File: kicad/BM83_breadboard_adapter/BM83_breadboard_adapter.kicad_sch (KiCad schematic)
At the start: 66 parts, among them J1 PJ-320B, J2 PJ-320B, J3 USB_B_Micro, J4 Conn_01x25_Female, J5 Conn_01x25_Female, J6 PJ-320B, SW1 VOL-, SW2 VOL+, SW3 REV, SW4 FWD, SW6 PLAY/PAUSE, SW7 SELECT, SW8 MFB, SW9 RESET, U1 BM83, U2 PJ-3027F

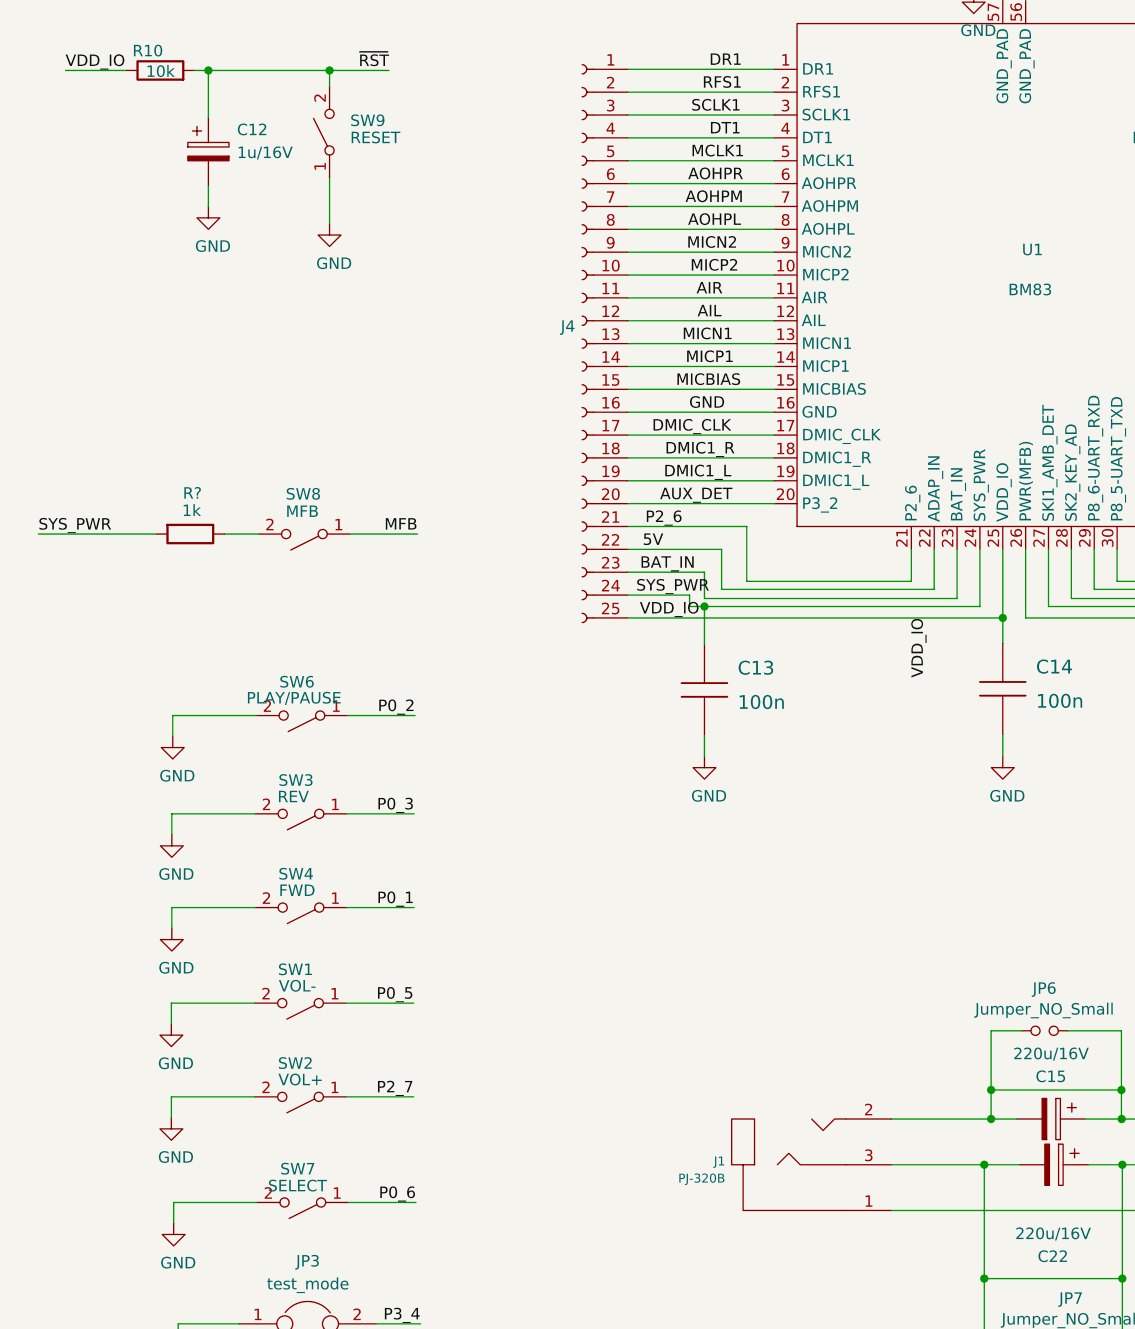
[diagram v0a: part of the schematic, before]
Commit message: update BM83 footprint on board!
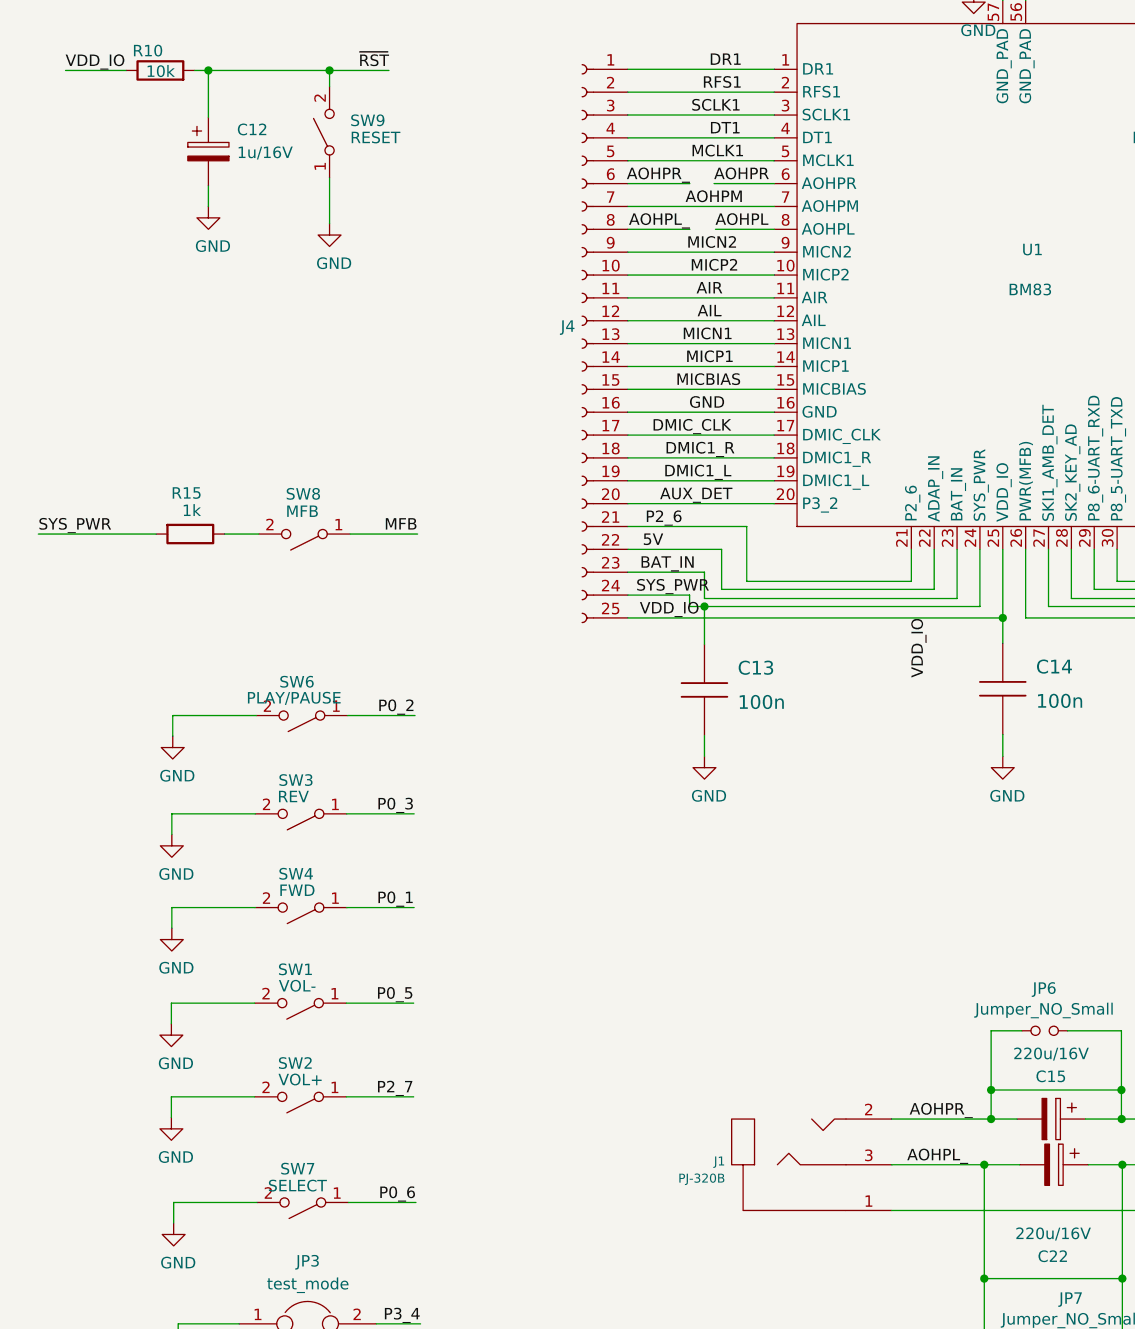
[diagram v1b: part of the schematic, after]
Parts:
- gave numbers to parts that had none: 1
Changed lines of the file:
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@@
     (stroke (width 0) (type solid) (color 0 0 0 0))
   )
-  (wire (pts (xy 294.7162 43.942) (xy 310.9722 43.942))
+  (wire (pts (xy 294.7162 43.942) (xy 301.5996 43.942))
     (stroke (width 0) (type solid) (color 0 0 0 0))
   )
@@
     (stroke (width 0) (type solid) (color 0 0 0 0))
   )
-  (wire (pts (xy 294.7162 49.022) (xy 310.9722 49.022))
+  (wire (pts (xy 294.7162 49.022) (xy 301.5996 49.022))
     (stroke (width 0) (type solid) (color 0 0 0 0))
   )
@@
   )
   (wire (pts (xy 303.2252 105.283) (xy 303.2252 107.569))
+    (stroke (width 0) (type solid) (color 0 0 0 0))
+  )
+  (wire (pts (xy 304.292 43.942) (xy 310.9722 43.942))
+    (stroke (width 0) (type solid) (color 0 0 0 0))
+  )
+  (wire (pts (xy 304.4444 49.022) (xy 310.9722 49.022))
     (stroke (width 0) (type solid) (color 0 0 0 0))
   )
@@
     (effects (font (size 1.27 1.27)) (justify right bottom))
   )
+  (label "AOHPR_" (at 301.5996 43.942 180)
+    (effects (font (size 1.27 1.27)) (justify right bottom))
+  )
+  (label "AOHPL_" (at 301.5996 49.022 180)
+    (effects (font (size 1.27 1.27)) (justify right bottom))
+  )
+  (label "AOHPR" (at 304.292 43.942 0)
+    (effects (font (size 1.27 1.27)) (justify left bottom))
+  )
+  (label "AOHPL" (at 304.4444 49.022 0)
+    (effects (font (size 1.27 1.27)) (justify left bottom))
+  )
   (label "AIL" (at 305.1302 59.182 180)
     (effects (font (size 1.27 1.27)) (justify right bottom))
@@
     (effects (font (size 1.27 1.27)) (justify right bottom))
   )
-  (label "AOHPL" (at 307.2892 49.022 180)
-    (effects (font (size 1.27 1.27)) (justify right bottom))
-  )
   (label "MICBIAS" (at 307.2892 66.802 180)
     (effects (font (size 1.27 1.27)) (justify right bottom))
@@
     (effects (font (size 1.27 1.27)) (justify right bottom))
   )
-  (label "AOHPR" (at 307.5432 43.942 180)
-    (effects (font (size 1.27 1.27)) (justify right bottom))
-  )
   (label "AOHPM" (at 307.5432 46.482 180)
     (effects (font (size 1.27 1.27)) (justify right bottom))
@@
   )
   (label "VDD_IO" (at 327.9902 92.202 270)
+    (effects (font (size 1.27 1.27)) (justify right bottom))
+  )
+  (label "AOHPL_" (at 332.5114 152.9588 180)
+    (effects (font (size 1.27 1.27)) (justify right bottom))
+  )
+  (label "AOHPR_" (at 333.0194 147.8788 180)
     (effects (font (size 1.27 1.27)) (justify right bottom))
   )
@@
   (symbol (lib_id "Device:R") (at 246.1006 82.8802 270) (unit 1)
     (in_bom yes)
-    (property "Reference" "R?" (id 0) (at 247.396 78.359 90)
+    (property "Reference" "R15" (id 0) (at 247.396 78.359 90)
       (effects (font (size 1.27 1.27)) (justify right))
     )
@@
     )
     (path "/f576e113-5805-49c9-a806-fa5db2c8effa"
-      (reference "R?") (unit 1)
+      (reference "R15") (unit 1)
     )
     (path "/90a9bce0-f150-4d9c-b6f9-eb56d5aefdaf"

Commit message: fixies
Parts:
- C1, C17, C18, C2, C20, C21, C3, C4: value 1u/16V -> (none); footprint Capacitors_SMD.pretty:C_1206_HandSoldering -> (none)
- C10: value 10uF/16V -> (none); footprint Capacitors_SMD.pretty:C_1206_HandSoldering -> (none)
- C11: value 10u/16V -> (none); footprint Capacitors_SMD.pretty:C_1206_HandSoldering -> (none)
- C12, C8: value 1u/16V -> (none); footprint Capacitors_Tantalum_SMD.pretty:TantalC_SizeA_EIA-3216_HandSoldering -> (none)
- C13, C14, C7, C9: value 100n -> (none); footprint Capacitors_SMD.pretty:C_0805_HandSoldering -> (none)
- C15, C22: value 220u/16V -> (none); footprint Capacitors_ThroughHole.pretty:C_Radial_D6.3_L11.2_P2.5 -> (none)
- C16, C19: value 220p -> (none); footprint Capacitors_SMD.pretty:C_0805_HandSoldering -> (none)
- C5, C6: value 470p -> (none); footprint Capacitors_SMD.pretty:C_0805_HandSoldering -> (none)
- D1, D2: value LED -> (none); footprint LEDs:LED_1206_HandSoldering -> (none)
- J1, J2, J6: value PJ-320B -> (none); footprint jacks:3.5mm_stereo_jack_PJ320B -> (none)
- J3: value USB_B_Micro -> (none); footprint Connect.pretty:USB_Micro-B -> (none)
- J4, J5: value Conn_01x25_Female -> (none); footprint Pin_Headers.pretty:Pin_Header_Straight_1x25 -> (none)
- JP1, JP4, JP6, JP7: value Jumper_NO_Small -> (none); footprint Jumper:SolderJumper-2_P1.3mm_Open_RoundedPad1.0x1.5mm -> (none)
- JP2, JP5: value single_end_mic -> (none); footprint Jumper:SolderJumper-2_P1.3mm_Open_RoundedPad1.0x1.5mm -> (none)
- JP3: value test_mode -> (none); footprint Pin_Headers.pretty:Pin_Header_Straight_1x02 -> (none)
- L1: value 30 -> (none); footprint Resistors_SMD.pretty:R_1206_HandSoldering -> (none)
- R1, R11, R12, R14, R15, R2, R3, R5: value 1k -> (none); footprint Resistors_SMD.pretty:R_0805_HandSoldering -> (none)
- R10, R6, R7: value 10k -> (none); footprint Resistors_SMD.pretty:R_0805_HandSoldering -> (none)
- R13, R4: value 2k -> (none); footprint Resistors_SMD.pretty:R_0805_HandSoldering -> (none)
- R8, R9: value 20 -> (none); footprint Resistors_SMD.pretty:R_0805_HandSoldering -> (none)
- RV1, RV2, RV3: value CG0603MLC-05E -> (none); footprint Resistors_SMD.pretty:R_0603_HandSoldering -> (none)
- SW1: value VOL- -> (none); footprint Buttons_Switches_SMD.pretty:SW_SPST_FSMSM -> (none)
- SW2: value VOL+ -> (none); footprint Buttons_Switches_SMD.pretty:SW_SPST_FSMSM -> (none)
- SW3: value REV -> (none); footprint Buttons_Switches_SMD.pretty:SW_SPST_FSMSM -> (none)
- SW4: value FWD -> (none); footprint Buttons_Switches_SMD.pretty:SW_SPST_FSMSM -> (none)
- SW6: value PLAY/PAUSE -> (none); footprint Buttons_Switches_SMD.pretty:SW_SPST_FSMSM -> (none)
- SW7: value SELECT -> (none); footprint Buttons_Switches_SMD.pretty:SW_SPST_FSMSM -> (none)
- SW8: value MFB -> (none); footprint Buttons_Switches_SMD.pretty:SW_SPST_FSMSM -> (none)
- SW9: value RESET -> (none); footprint Buttons_Switches_SMD.pretty:SW_SPST_FSMSM -> (none)
- U1: value BM83 -> (none); footprint bluetooth:BM83 -> (none)
- U2: value PJ-3027F -> (none); footprint jacks:PJ-327A -> (none)
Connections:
- net ~RST renamed ~{RST}

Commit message: update
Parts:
- C1, C17, C18, C2, C20, C21, C3, C4: value (none) -> 1u/16V; footprint (none) -> Capacitors_SMD.pretty:C_1206_HandSoldering
- C10: value (none) -> 10uF/16V; footprint (none) -> Capacitors_SMD.pretty:C_1206_HandSoldering
- C11: value (none) -> 10u/16V; footprint (none) -> Capacitors_SMD.pretty:C_1206_HandSoldering
- C12, C8: value (none) -> 1u/16V; footprint (none) -> Capacitors_Tantalum_SMD.pretty:TantalC_SizeA_EIA-3216_HandSoldering
- C13, C14, C7, C9: value (none) -> 100n; footprint (none) -> Capacitors_SMD.pretty:C_0805_HandSoldering
- C15, C22: value (none) -> 220u/16V; footprint (none) -> Capacitors_ThroughHole.pretty:C_Radial_D6.3_L11.2_P2.5
- C16, C19: value (none) -> 220p; footprint (none) -> Capacitors_SMD.pretty:C_0805_HandSoldering
- C5, C6: value (none) -> 470p; footprint (none) -> Capacitors_SMD.pretty:C_0805_HandSoldering
- D1, D2: value (none) -> LED; footprint (none) -> LEDs:LED_1206_HandSoldering
- J1, J2, J6: value (none) -> PJ-320B; footprint (none) -> jacks:3.5mm_stereo_jack_PJ320B
- J3: value (none) -> USB_B_Micro; footprint (none) -> Connect.pretty:USB_Micro-B
- J4, J5: value (none) -> Conn_01x25_Female; footprint (none) -> Pin_Headers.pretty:Pin_Header_Straight_1x25
- JP1, JP4, JP6, JP7: value (none) -> Jumper_NO_Small; footprint (none) -> Jumper:SolderJumper-2_P1.3mm_Open_RoundedPad1.0x1.5mm
- JP2, JP5: value (none) -> single_end_mic; footprint (none) -> Jumper:SolderJumper-2_P1.3mm_Open_RoundedPad1.0x1.5mm
- JP3: value (none) -> test_mode; footprint (none) -> Pin_Headers.pretty:Pin_Header_Straight_1x02
- L1: value (none) -> 30; footprint (none) -> Resistors_SMD.pretty:R_1206_HandSoldering
- R1, R11, R12, R14, R15, R2, R3, R5: value (none) -> 1k; footprint (none) -> Resistors_SMD.pretty:R_0805_HandSoldering
- R10, R6, R7: value (none) -> 10k; footprint (none) -> Resistors_SMD.pretty:R_0805_HandSoldering
- R13, R4: value (none) -> 2k; footprint (none) -> Resistors_SMD.pretty:R_0805_HandSoldering
- R8, R9: value (none) -> 20; footprint (none) -> Resistors_SMD.pretty:R_0805_HandSoldering
- RV1, RV2, RV3: value (none) -> CG0603MLC-05E; footprint (none) -> Resistors_SMD.pretty:R_0603_HandSoldering
- SW1: value (none) -> VOL-; footprint (none) -> Buttons_Switches_SMD.pretty:SW_SPST_FSMSM
- SW2: value (none) -> VOL+; footprint (none) -> Buttons_Switches_SMD.pretty:SW_SPST_FSMSM
- SW3: value (none) -> REV; footprint (none) -> Buttons_Switches_SMD.pretty:SW_SPST_FSMSM
- SW4: value (none) -> FWD; footprint (none) -> Buttons_Switches_SMD.pretty:SW_SPST_FSMSM
- SW6: value (none) -> PLAY/PAUSE; footprint (none) -> Buttons_Switches_SMD.pretty:SW_SPST_FSMSM
- SW7: value (none) -> SELECT; footprint (none) -> Buttons_Switches_SMD.pretty:SW_SPST_FSMSM
- SW8: value (none) -> MFB; footprint (none) -> Buttons_Switches_SMD.pretty:SW_SPST_FSMSM
- SW9: value (none) -> RESET; footprint (none) -> Buttons_Switches_SMD.pretty:SW_SPST_FSMSM
- U1: value (none) -> BM83; footprint (none) -> bluetooth:BM83
- U2: value (none) -> PJ-3027F; footprint (none) -> jacks:PJ-327A
